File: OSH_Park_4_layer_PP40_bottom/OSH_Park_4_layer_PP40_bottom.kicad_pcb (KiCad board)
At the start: 2 copper layers, 45.5 x 32 mm, 7 parts, among them J1 PINS_1X12, J2 PINS_1X12

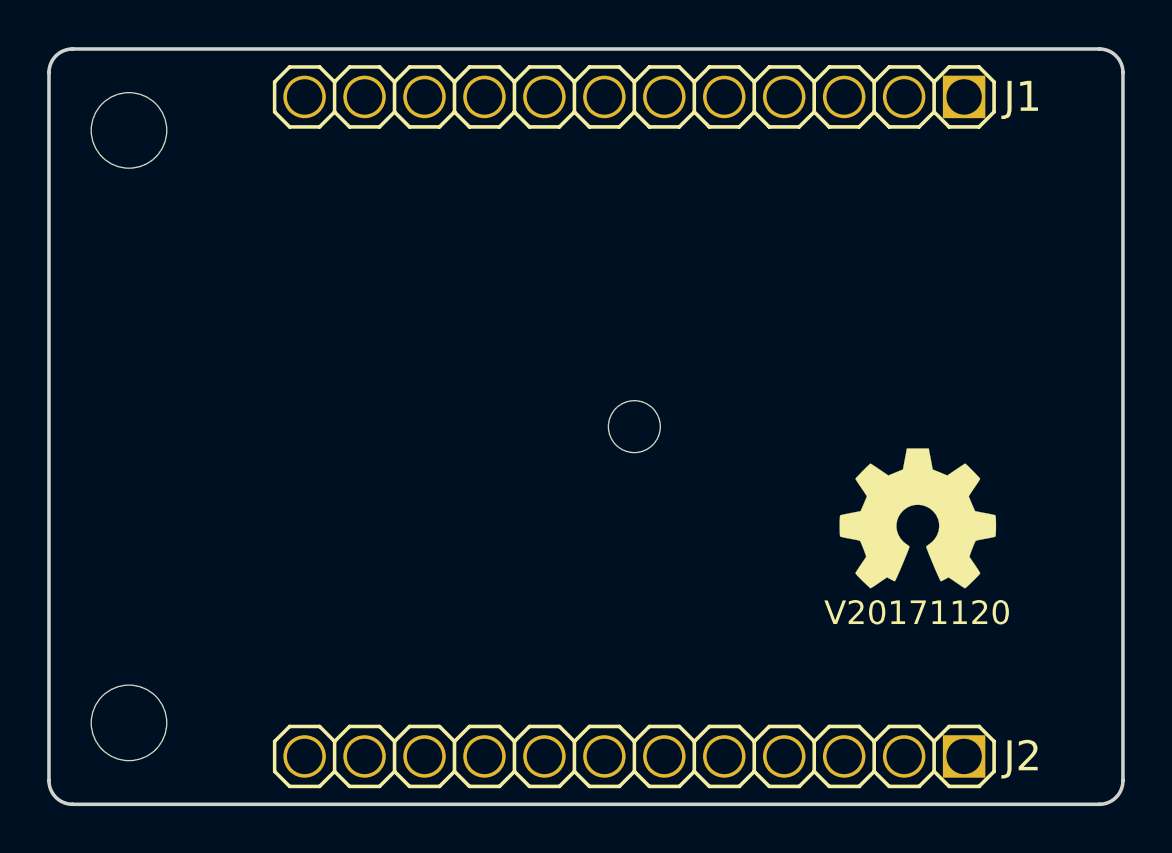
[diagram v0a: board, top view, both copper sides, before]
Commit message: * removed orphan footprints
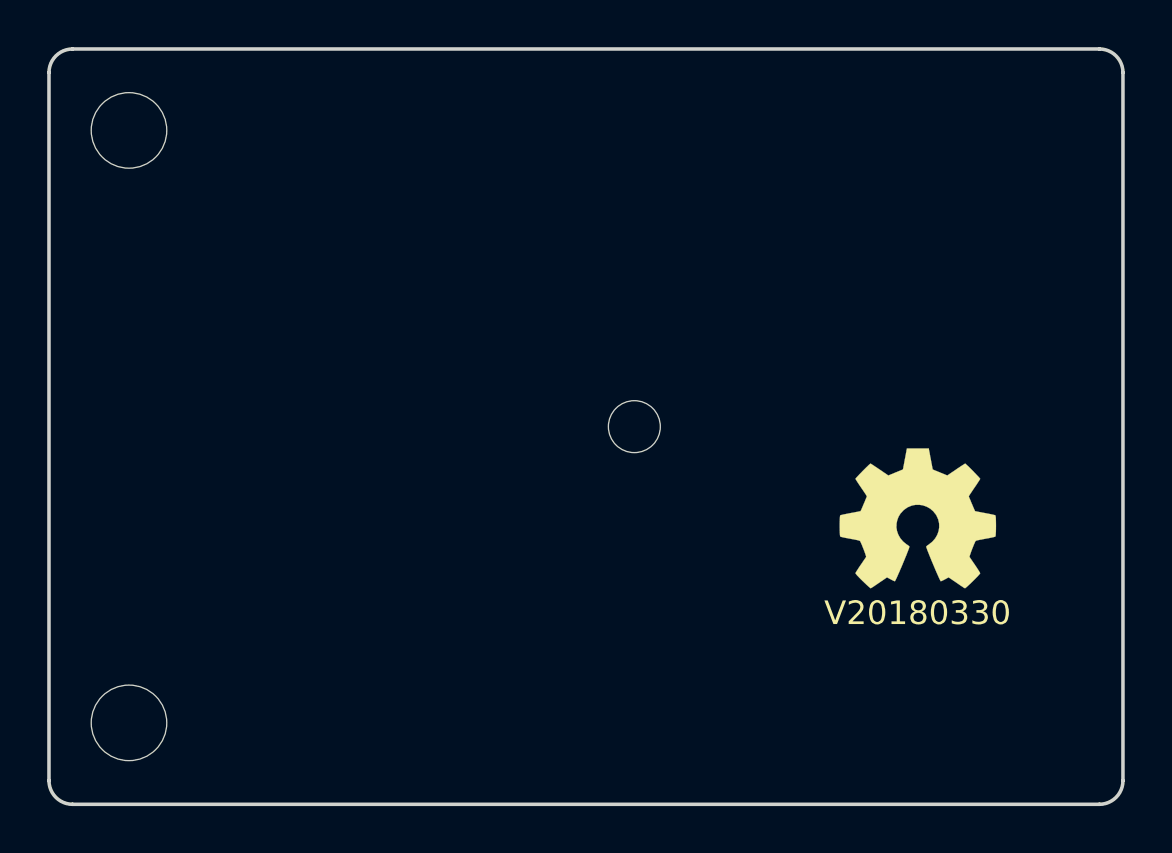
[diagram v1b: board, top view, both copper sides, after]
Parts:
- removed J1, J2: PINS_1X12, SquantorConnectors:Header-0254-1X12-H015
- N2: value V20171120 -> V20180330

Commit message: * added 4 layer OSHpark design rules
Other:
- copper layers 2 -> 4
- net class Default: clearance 0.1524 -> 0.127; trace_width 0.1524 -> 0.127
- rule trace_clearance: 0.1524 -> 0.127
- rule trace_min: 0.1524 -> 0.127
- rule via_min_size: 0.381 -> 0.3556
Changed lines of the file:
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@@
     (links 0)
     (no_connects 0)
-    (area 123.124999 85.024999 168.775001 117.175001)
+    (area 119.056646 84.6226 168.775001 117.6774)
     (thickness 1.6)
     (drawings 8)
@@
   (layers
     (0 F.Cu signal)
+    (1 In1.Cu signal)
+    (2 In2.Cu signal)
     (31 B.Cu signal)
     (32 B.Adhes user)
@@
   )
   (setup
-    (last_trace_width 0.1524)
-    (user_trace_width 0.1524)
+    (last_trace_width 0.127)
+    (user_trace_width 0.127)
     (user_trace_width 0.2)
     (user_trace_width 0.3)
@@
     (user_trace_width 1.5)
     (user_trace_width 2)
-    (trace_clearance 0.1524)
+    (trace_clearance 0.127)
     (zone_clearance 0.508)
     (zone_45_only no)
-    (trace_min 0.1524)
+    (trace_min 0.127)
     (segment_width 0.2)
     (edge_width 0.15)
     (via_size 0.381)
     (via_drill 0.254)
-    (via_min_size 0.381)
+    (via_min_size 0.3556)
     (via_min_drill 0.254)
-    (user_via 0.381 0.254)
+    (user_via 0.3556 0.254)
     (user_via 0.55 0.4)
     (user_via 0.75 0.6)
@@
   (net 0 "")
   (net_class Default "This is the default net class."
-    (clearance 0.1524)
-    (trace_width 0.1524)
+    (clearance 0.127)
+    (trace_width 0.127)
     (via_dia 0.381)
     (via_drill 0.254)
